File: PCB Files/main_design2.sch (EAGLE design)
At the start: 41 parts, among them IC1 7805TV, IC2 MCP73831

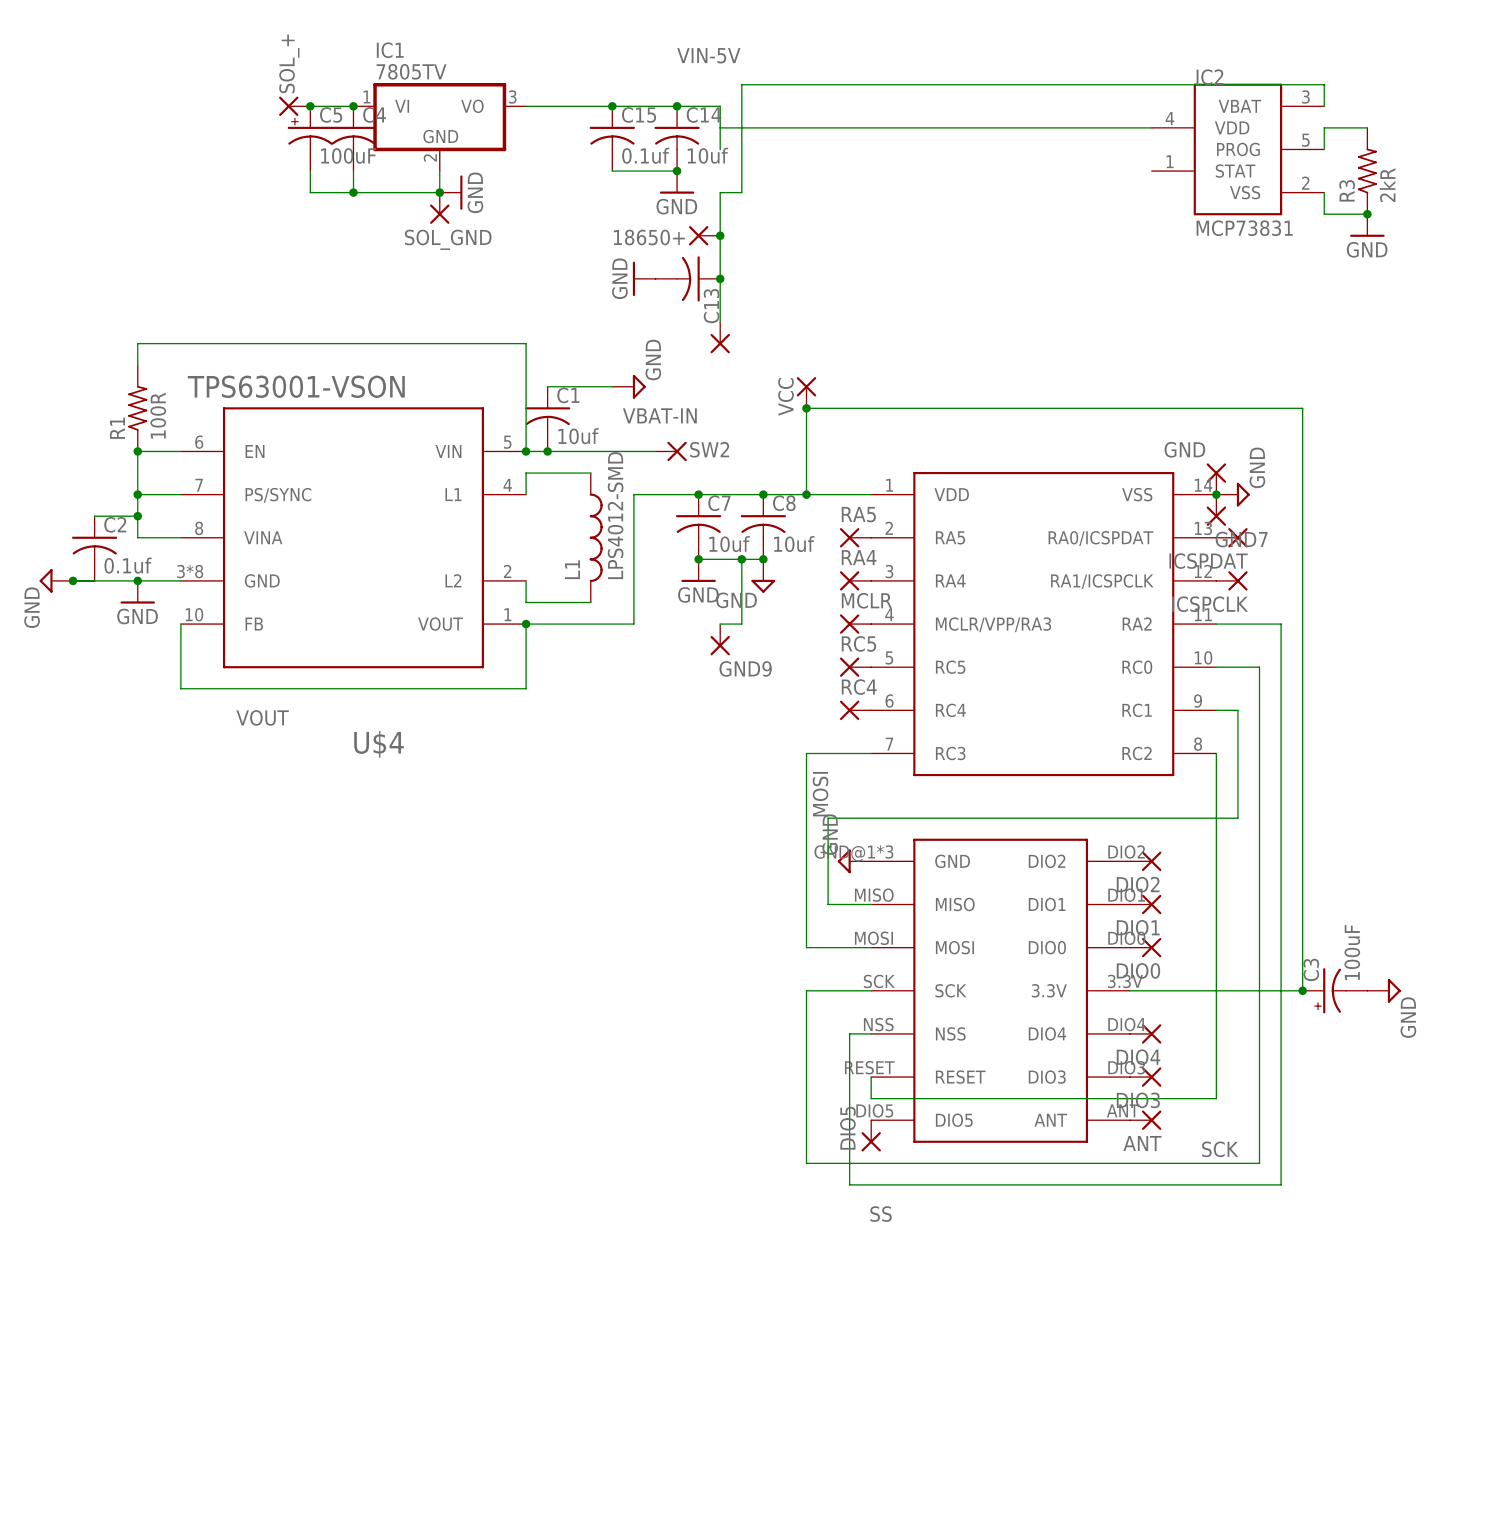
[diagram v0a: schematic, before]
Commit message: 9.19 new PCB and code is working. currently set to standard power, not H-power versions of RFM69.
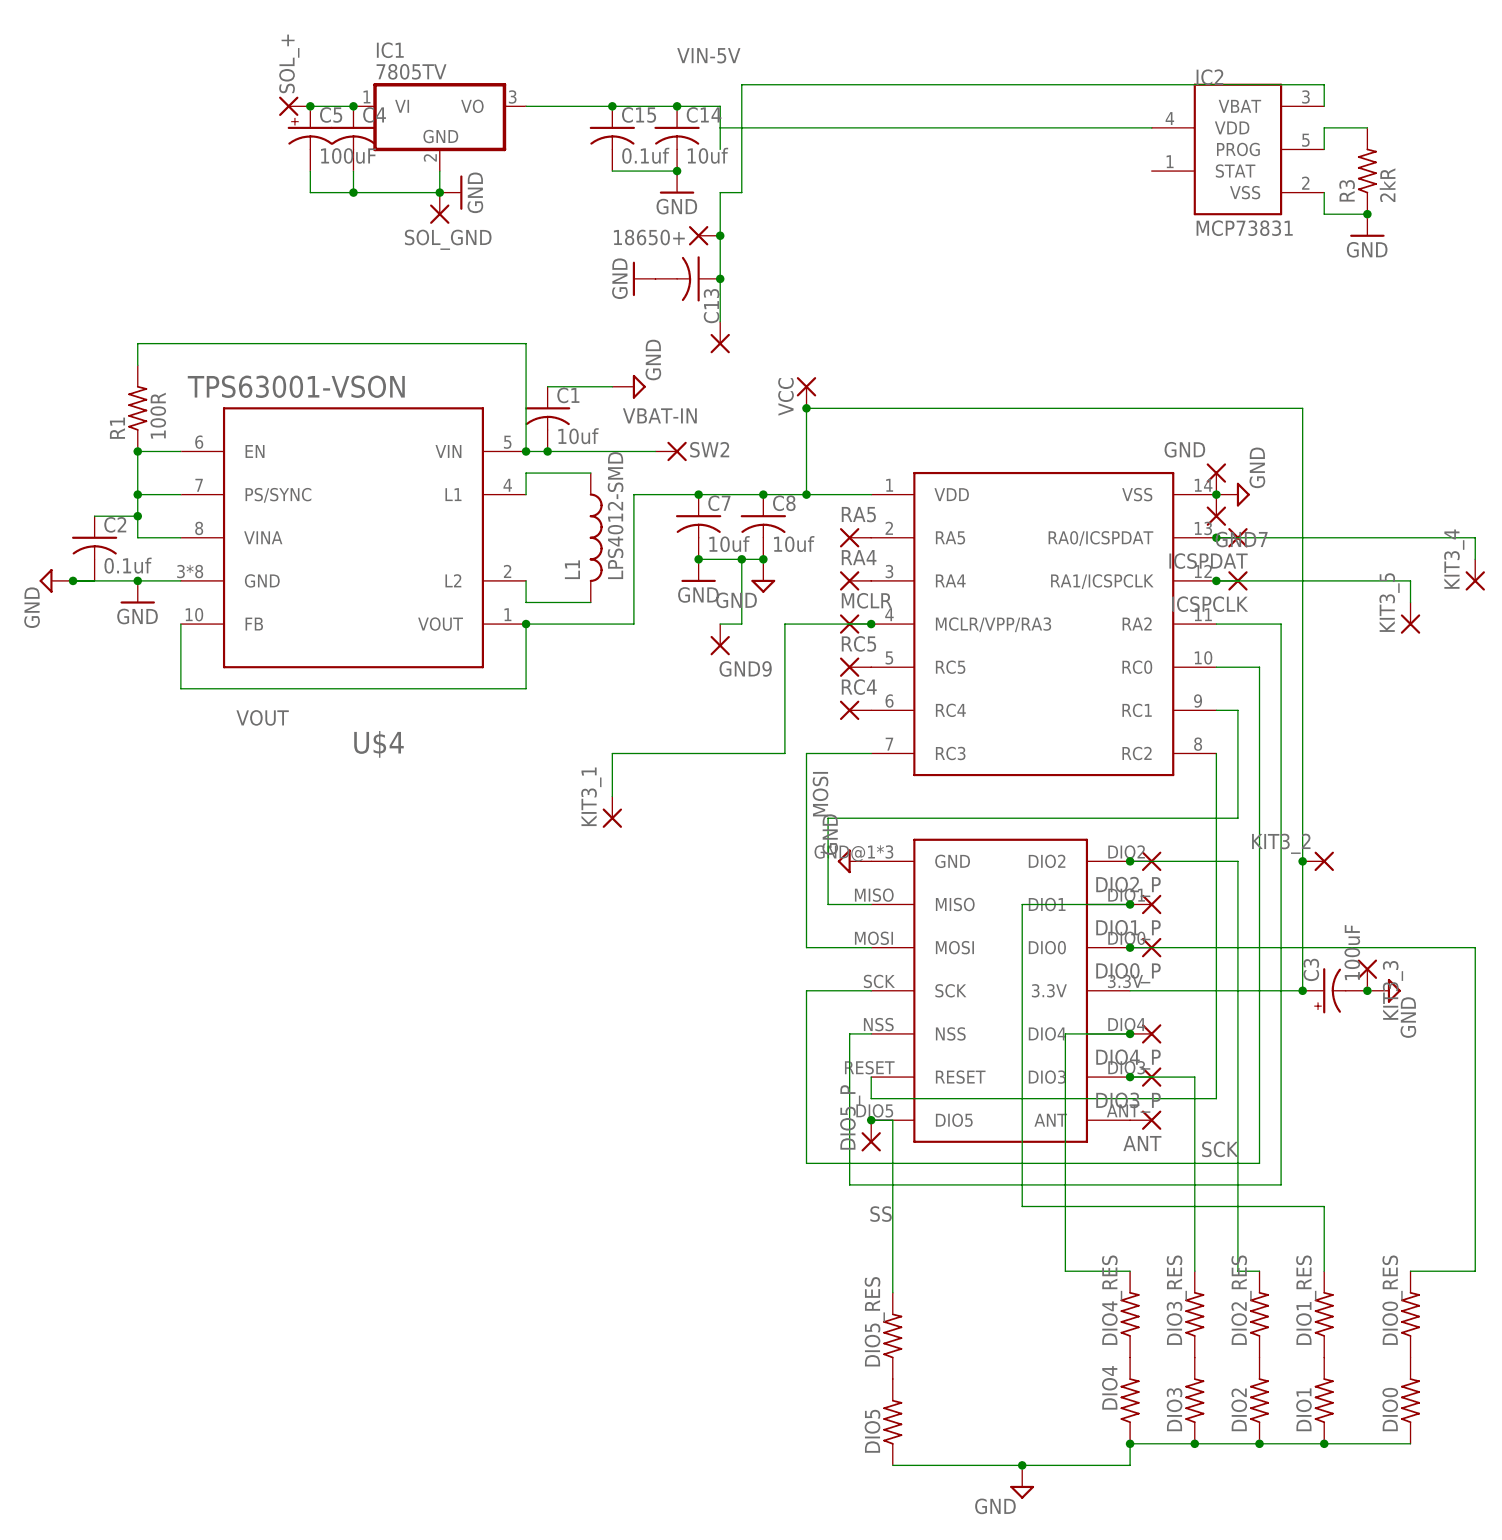
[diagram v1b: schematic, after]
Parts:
- added DIO0_P, DIO1_P, DIO2_P, DIO3_P, DIO4_P, DIO5_P, KIT3_1, KIT3_2, KIT3_3, KIT3_4, KIT3_5: (no value), wirepad:1,6/0,8
- added DIO0_RES, DIO1_RES, DIO2_RES, DIO3_RES, DIO4_RES, DIO5_RES: (no value), rcl:R-US_R0805
- DIO0, DIO1, DIO2, DIO3, DIO4, DIO5: device wirepad:1,6/0,8 -> rcl:R-US_R0805
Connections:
- removed net N$18: DIO3.P, U$3.DIO3
- new net N$11: DIO5.2, DIO5_RES.1
- new net N$23: DIO4.2, DIO4_RES.1
- new net N$24: DIO3.2, DIO3_RES.1
- new net N$25: DIO0.2, DIO0_RES.1
- new net N$26: DIO2.2, DIO2_RES.1
- new net N$28: DIO3_P.P, DIO3_RES.2, U$3.DIO3
- new net N$5: DIO1.2, DIO1_RES.1
- net GND: now also DIO0.1, DIO1.1, DIO2.1, DIO3.1, DIO4.1, DIO5.1, KIT3_3.P
- net N$12: now also KIT3_5.P
- net N$13: now also KIT3_4.P
- net N$14: now also KIT3_1.P
- net N$15: now also DIO1_P.P, DIO1_RES.2; no longer DIO1.P
- net N$16: now also DIO0_P.P, DIO0_RES.2; no longer DIO0.P
- net N$17: now also DIO4_P.P, DIO4_RES.2; no longer DIO4.P
- net N$20: now also DIO5_P.P, DIO5_RES.2; no longer DIO5.P
- net N$9: now also DIO2_P.P, DIO2_RES.2; no longer DIO2.P
- net VOUT: now also KIT3_2.P
